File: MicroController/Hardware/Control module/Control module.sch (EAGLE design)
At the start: 101 parts, among them IC1 MCP1703CB, J1 1X2-3.5MM, J2 0446200002, J3 0446200002, J4 0446200002, Q1 BSS138, Q10 BSS138, Q11 BSS138, Q12 BSS138, Q2 BSS138, Q3 BSS138, Q4 BSS138, Q5 BSS138, Q6 BSS138, Q7 BSS138, Q8 BSS138, Q9 BSS138, U1 CD74HC4067SM96, U2 7812DT, U3 TLV1117-33CDCY, U4 CD4051BM

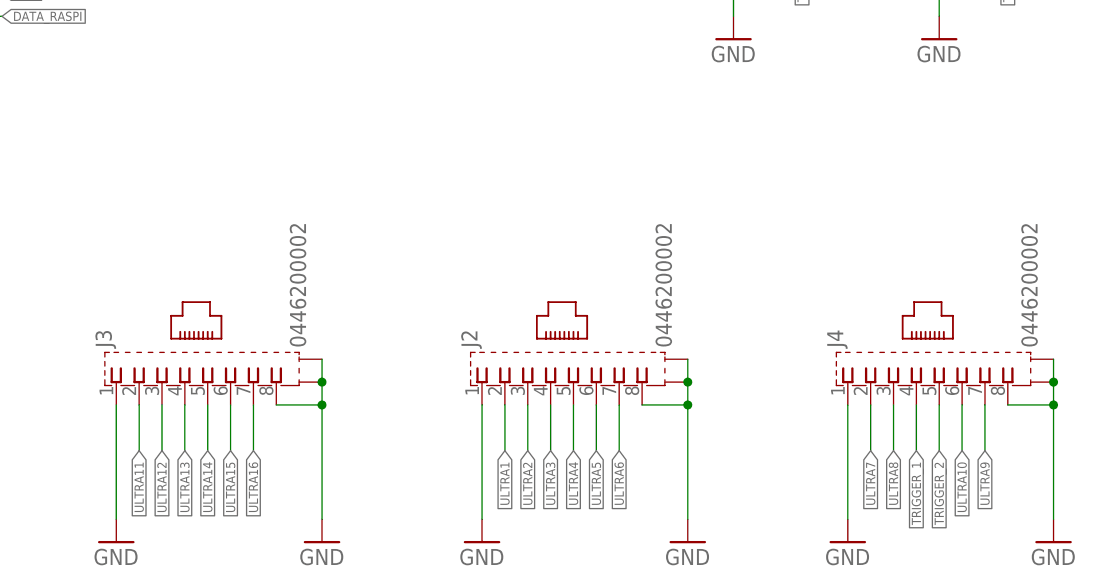
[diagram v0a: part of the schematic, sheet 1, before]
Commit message: Started a redesign of the Distance sensor PCB.
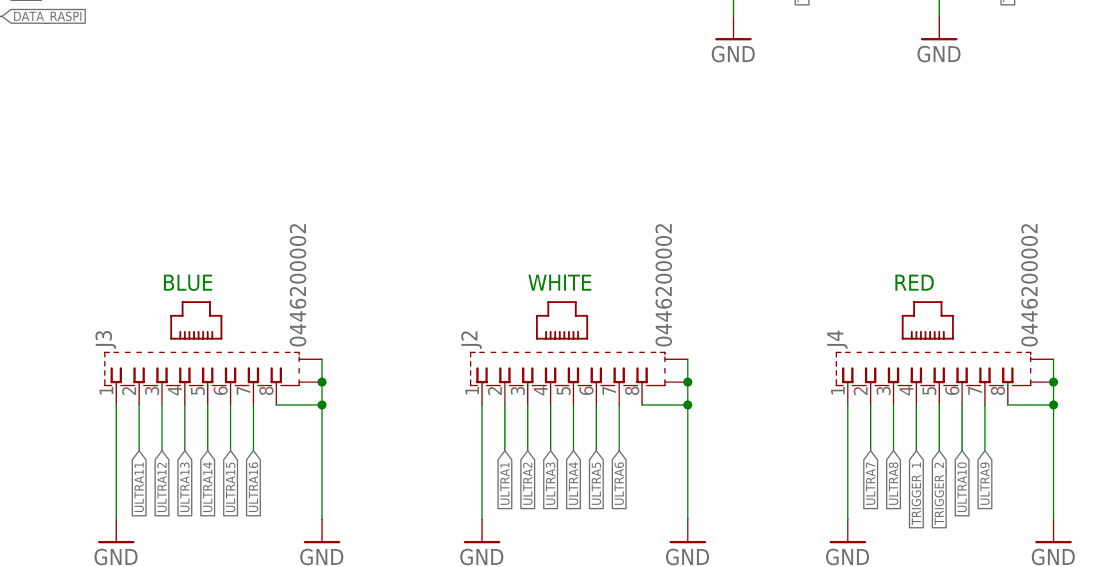
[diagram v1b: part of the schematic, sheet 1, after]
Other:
- note added: "BLUE"
- note added: "RED"
- note added: "WHITE"
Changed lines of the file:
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@@
 <text x="-2.54" y="200.66" size="1.778" layer="91">+</text>
 <text x="-2.54" y="198.12" size="1.778" layer="91">-</text>
+<text x="20.32" y="5.08" size="1.778" layer="91">BLUE</text>
+<text x="60.96" y="5.08" size="1.778" layer="91">WHITE</text>
+<text x="101.6" y="5.08" size="1.778" layer="91">RED</text>
 </plain>
 <instances>

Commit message: Started working on the next revision of the Control PCB.
Work in progress. The notes on the hardware can be found in the documentation.
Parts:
- removed C19, C20, C21, C22: 100nF, adafruit:C-USC0603
- removed FAN_1, FAN_2: JST-PH_2-PIN_HEADER, SRG:JST-PH_2-PIN_HEADER
- removed FUSE: 6V/0.5A, SparkFun-Fuses:PPTC_HALF-AMP
- removed JUMPER: (no value), jumper:JP2Q
- removed RASPBERRY: RJ11, SparkFun-Connectors:RJ11-6
- added C24: 100nF, adafruit:C-USC0805
- added FUSE1: 6V/0.5A, SparkFun-Fuses:PPTC_HALF-AMP
- added J5: 0446200002, con-molex:0446200002
- added U5: TB6621FNG, SparkFun:TB6621FNG
- added U6, U7: TXB0108PWR, Texas Instruments_By_element14_Batch_1:TXB0108PWR
- C11, C12, C13, C14, C15, C16, C17, C18: device adafruit:C-USC0603 -> adafruit:C-USC1206
- R23, R24, R25: device SparkFun:RESISTOR0603-RES -> adafruit:R-US_R0805
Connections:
- removed net DATA_RASPI: JUMPER.2, RASPBERRY.1
- removed net RES_RASPI: JUMPER.4, RASPBERRY.4
- removed net ULTRA10: J4.6, U1.CHAN4
- removed net ULTRA9: J4.7, U1.CHAN5
- new net N$10: U7.A7
- new net N$11: U7.A8
- new net N$4: U7.A1
- new net N$5: U7.A2
- new net N$6: U7.A3
- new net N$7: U7.A4
- new net N$8: U7.A5
- new net N$9: U7.A6
- new net ULTRAS1: J4.2, U6.B1
- new net ULTRAS10: U7.B2
- new net ULTRAS11: U7.B3
- new net ULTRAS12: U7.B4
- new net ULTRAS13: U7.B5
- new net ULTRAS14: U7.B6
- new net ULTRAS15: U7.B7
- new net ULTRAS16: U7.B8
- new net ULTRAS2: J4.3, U6.B2
- new net ULTRAS3: J4.4, U6.B3
- new net ULTRAS4: J4.5, U6.B4
- new net ULTRAS5: J4.6, U6.B5
- new net ULTRAS6: J4.7, U6.B6
- new net ULTRAS7: J2.2, U6.B7
- new net ULTRAS8: J2.3, U6.B8
- new net ULTRAS9: U7.B1
- net +12V: now also C24.1
- net +24V: now also FUSE1.2; no longer FUSE.2
- net A: now also U$1.PF2(OC0C/RXD0); no longer U$1.PE7(TOSC1/CKOUT/EVO/TXD1/SCK)
- net B: now also U$1.PF1(OC0B/XCK0); no longer U$1.PE6(TOSC2/RXD1/MISO)
- net C: now also U$1.PF0(OC0A); no longer U$1.PE5(OC1B/XCK1/MOSI)
- net FAN_1_CONTROL: now also U5.PWMA; no longer FAN_1.2
- net FAN_2_CONTROL: now also U5.PWMB; no longer FAN_2.2
- net GND: now also C24.2, J5.1, J5.3, J5.5, J5.7, J5.S1, J5.S2, U5.GND, U6.GND, U7.GND; no longer C19.2, C20.2, C21.2, C22.2, FAN_1.1, FAN_2.1, RASPBERRY.2
- net IR_3: now also U$1.PA2(ADC2/AC2)
- net IR_4: now also U$1.PA3(ADC3/AC3)
- net IR_5: no longer U$1.PA2(ADC2/AC2)
- net IR_6: no longer U$1.PA3(ADC3/AC3)
- net LED_1: now also U$1.PF3(OC0D/TXD0); no longer U$1.PD4(OC1A/SS)
- net LED_2: now also U$1.PF4; no longer U$1.PD5(OC1B/XCK1/MOSI)
- net MOTOR_LEVEL_3: now also U4.6; no longer U4.4
- net MOTOR_LEVEL_4: now also U4.4; no longer U4.6
- net PDI_DATA: no longer JUMPER.1
- net RESET_PDI_CLK: no longer JUMPER.3
- net RX_RASPI: now also J5.4; no longer RASPBERRY.5
- net TEMP_1: now also U$1.PD6(RXD1/MISO); no longer U$1.PF3(OC0D/TXD0)
- net TEMP_2: now also U$1.PD5(OC1B/XCK1/MOSI); no longer U$1.PF4
- net TEMP_3: now also U$1.PD4(OC1A/SS); no longer U$1.PF5
- net TRIGGER_1: no longer J4.4
- net TRIGGER_2: no longer J4.5
- net TX_RASPI: now also J5.6; no longer RASPBERRY.3
- net ULTRA1: now also U1.CHAN0, U6.A1; no longer J2.2, U1.CHAN3
- net ULTRA11: no longer U1.CHAN10
- net ULTRA2: now also U1.CHAN1, U6.A2; no longer J2.3, U1.CHAN2
- net ULTRA3: now also U1.CHAN2, U6.A3; no longer U1.CHAN1
- net ULTRA4: now also U1.CHAN3, U6.A4; no longer U1.CHAN0
- net ULTRA5: now also U1.CHAN4, U6.A5; no longer U1.CHAN8
- net ULTRA6: now also U1.CHAN5, U6.A6; no longer U1.CHAN9
- net ULTRA7: now also U6.A7; no longer J4.2, U1.CHAN7
- net ULTRA8: now also U6.A8; no longer J4.3, U1.CHAN6
- net VCC: now also J5.2, J5.8, U6.OE, U6.VCCA, U7.OE, U7.VCCA; no longer C19.1, C20.1, C21.1, C22.1, RASPBERRY.6
- net VIN: now also FUSE1.1; no longer FUSE.1
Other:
- moved on the sheet: C1, C10, C11, C12, C13, C14, C15, C16, C17, C18, C2, C23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

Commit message: Control PCB revision 2 is now complete.
A lot of changes compared to the first revision. Most noticable the layout of the connectors and the addition of the motor driver.
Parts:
- removed IC1: MCP1703CB, linear:MCP1703CB
- removed IR_1, IR_2, IR_3, IR_4, IR_5, IR_6, IR_7, IR_8: JST-PH_3-PIN_HEADER, SRG:JST-PH_3-PIN_HEADER
- removed MOTOR_1, MOTOR_2, MOTOR_3, MOTOR_4, MOTOR_5, MOTOR_6, MOTOR_7, MOTOR_8: JST-PH_2-PIN_HEADER, SRG:JST-PH_2-PIN_HEADER
- removed U$1: XMEGA-A3-AU, SparkFun-Retired:XMEGA-A3-AU
- added 12V, FAN_1, FAN_2: 1X2-3.5MM, adafruit:1X2-3.5MM
- added C19, C20, C21, C25, C26: 1.0uF, SparkFun-Capacitors:1.0UF-0805-25V-(+80/-20%)
- added C22: 1.0uF, SparkFun-Capacitors:1.0UF-0805-25V-10%
- added FUSE2: 6V/0.5A, SparkFun-Fuses:PPTC_HALF-AMP
- added LED3: (no value), adafruit:LEDCHIPLED_0805
- added MOTOR1, MOTOR2, MOTOR3, MOTOR4, MOTOR5, MOTOR6, MOTOR7, MOTOR8: 22-05-7028-02, con-molex:22-05-7028-02
- added R30: 330, adafruit:R-US_R0805
- added SENSOR1, SENSOR2, SENSOR3, SENSOR4, SENSOR5, SENSOR6, SENSOR7, SENSOR8: 22-05-7038-03, con-molex:22-05-7038-03
- added U8: LM2937IMP-5.0, NSC_By_element14_Batch_1.1:LM2937IMP-5.0
- added U9: CD74HC4067SM96, SparkFun-IC-Logic:74HC4067SM96
- C10, C6, C7, C8, C9: value 100nF -> 1.0uF; device adafruit:C-USC0805 -> SparkFun-Capacitors:1.0UF-0805-25V-(+80/-20%)
- C11, C12, C13, C14, C15, C16, C17, C18: value 100nF -> 1.0uF; device adafruit:C-USC1206 -> SparkFun-Capacitors:1.0UF-0805-25V-10%
- C2: value 220pF -> 1.0uF; device adafruit:C-USC1206 -> SparkFun-Capacitors:1.0UF-0805-25V-10%
- C24: value 100nF -> 1.0uF; device adafruit:C-USC0805 -> SparkFun-Capacitors:1.0UF-0805-25V-10%
- C3: value 100nF -> 1.0uF; device adafruit:C-USC1206 -> SparkFun-Capacitors:1.0UF-0805-25V-(+80/-20%)
- LED1, LED2: device led:LEDCHIPLED_0805 -> adafruit:LEDCHIPLED_0805
- U1: value CD74HC4067SM96 -> XMEGA-A3-AU; device SparkFun-IC-Logic:74HC4067SM96 -> SparkFun-Retired:XMEGA-A3-AU
- renumbered J1 to 24V, J5 to COMMUNICATION
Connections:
- removed net MOTOR_CONTROL: U$1.PD3(OX0D/TXD0), U4.COM_OUT/IN
- removed net N$10: U7.A7
- removed net N$11: U7.A8
- removed net N$5: U7.A2
- removed net N$6: U7.A3
- removed net N$8: U7.A5
- removed net N$9: U7.A6
- new net 12V_FANS: C22.1, C24.1, FUSE2.2, U5.VM1, U5.VM2, U5.VM3
- new net FAN_1+: FAN_1.1, U5.B01@11, U5.B01@12
- new net FAN_1-: FAN_1.2, U5.B02@7, U5.B02@8
- new net FAN_2+: FAN_2.2, U5.A01@1, U5.A01@2
- new net FAN_2-: FAN_2.1, U5.A02@5, U5.A02@6
- new net LED_3: R30.2, U1.PF5
- new net MOTOR_PWM: U1.PD1(OC0B/XCK0), U4.COM_OUT/IN
- new net ULTRA10: U7.A2, U9.CHAN9
- new net ULTRA9: U7.A1, U9.CHAN8
- net +12V: now also C19.1, C21.1, COMMUNICATION.2, U8.VIN; no longer C24.1, IC1.VI
- net +5V: now also C20.1, J2.5, J2.6, U6.VCCB, U7.VCCB, U8.VOUT; no longer IC1.VO
- net A: now also U1.PF2(OC0C/RXD0); no longer U$1.PF2(OC0C/RXD0)
- net B: now also U1.PF1(OC0B/XCK0); no longer U$1.PF1(OC0B/XCK0)
- net C: now also U1.PF0(OC0A); no longer U$1.PF0(OC0A)
- net FAN_1_CONTROL: now also U1.PC0(OC0A/OC0AL/SDA); no longer U$1.PC1(OC0B/AC0AH/XCK0/SCL)
- net FAN_2_CONTROL: now also U1.PC1(OC0B/AC0AH/XCK0/SCL); no longer U$1.PC0(OC0A/OC0AL/SDA)
- net GND: now also 12V.1, C19.2, C20.2, C21.2, C22.2, C25.2, C26.2, LED3.C, MOTOR1-1.S, MOTOR2-1.S, MOTOR3-1.S, MOTOR4-1.S, MOTOR5-1.S, MOTOR6-1.S, MOTOR7-1.S, MOTOR8-1.S, SENSOR1-2.S, SENSOR2-2.S, SENSOR3-2.S, SENSOR4-2.S, SENSOR5-2.S, SENSOR6-2.S, SENSOR7-2.S, SENSOR8-2.S, U1.AGND, U1.GND1, U1.GND2, U1.GND3, U1.GND4, U1.GND5, U5.AIN2, U5.BIN2, U5.PGND1@3, U5.PGND1@4, U5.PGND2@10, U5.PGND2@9, U8.GND, U8.GND_(TAB), U9.EN, U9.GND; no longer IC1.GND, IR_1.2, IR_2.2, IR_3.2, IR_4.2, IR_5.2, IR_6.2, IR_7.2, IR_8.2, J2.1, J2.8, MOTOR_1.1, MOTOR_2.1, MOTOR_3.1, MOTOR_4.1, MOTOR_5.1, MOTOR_6.1, MOTOR_7.1, MOTOR_8.1, U$1.AGND, U$1.GND1, U$1.GND2, U$1.GND3, U$1.GND4, U$1.GND5, U1.EN, U1.GND
- net IR_1: now also SENSOR1-1.S, U1.PA0(ADC0/AC0/AREF); no longer IR_1.1, U$1.PA0(ADC0/AC0/AREF)
- net IR_2: now also SENSOR2-1.S, U1.PA1(ADC1/AC1); no longer IR_2.1, U$1.PA1(ADC1/AC1)
- net IR_3: now also SENSOR3-1.S, U1.PB2(ADC2/AC2/DAC0); no longer IR_3.1, U$1.PA2(ADC2/AC2), U$1.PA4(ADC4/AC4)
- net IR_4: now also SENSOR4-1.S, U1.PB3(ADC3/AC3/DAC1); no longer IR_4.1, U$1.PA3(ADC3/AC3), U$1.PA5(ADC5/AC5)
- net IR_5: now also SENSOR5-1.S, U1.PB4(ADC4/AC4/TMS); no longer IR_5.1
- net IR_6: now also SENSOR6-1.S, U1.PB5(ADC5/AC5/TDI); no longer IR_6.1
- net IR_7: now also SENSOR7-1.S, U1.PB6(ADC6/AC6/TCK); no longer IR_7.1, U$1.PA6(ADC6/AC6)
- net IR_8: now also SENSOR8-1.S, U1.PB7(ADC7/AC7/AC0OUT/TDO); no longer IR_8.1, U$1.PA7(ADC7/AC7/AC0OUT)
- net LED_1: now also U1.PF3(OC0D/TXD0); no longer U$1.PF3(OC0D/TXD0)
- net LED_2: now also U1.PF4; no longer U$1.PF4
- net MOTOR_1: now also MOTOR1-2.S; no longer MOTOR_1.2
- net MOTOR_2: now also MOTOR2-2.S; no longer MOTOR_2.2
- net MOTOR_3: now also MOTOR3-2.S; no longer MOTOR_3.2
- net MOTOR_4: now also MOTOR4-2.S; no longer MOTOR_4.2
- net MOTOR_5: now also MOTOR5-2.S; no longer MOTOR_5.2
- net MOTOR_6: now also MOTOR6-2.S; no longer MOTOR_6.2
- net MOTOR_7: now also MOTOR7-2.S; no longer MOTOR_7.2
- net MOTOR_8: now also MOTOR8-2.S; no longer MOTOR_8.2
- net N$4: now also LED3.A, R30.1; no longer U7.A1
- net N$7: now also 12V.2, FUSE2.1; no longer U7.A4
- net PDI_DATA: now also U1.PDI_DATA; no longer U$1.PDI_DATA
- net RESET_PDI_CLK: now also U1./RESET_PDI_CLK; no longer U$1./RESET_PDI_CLK
- net RX_ATXMEGA: now also U1.PD2(OC0C/RXD0); no longer U$1.PC2(OC0C/OC0BL/RXD0)
- net S0: now also U1.PC7(OC0DH/CKOUT/EVO/TXD1/SCK), U9.S0; no longer U$1.PC7(OC0DH/CKOUT/EVO/TXD1/SCK), U1.S0
- net S1: now also U1.PC6(OC0DL/RXD1/MISO), U9.S1; no longer U$1.PC6(OC0DL/RXD1/MISO), U1.S1
- net S2: now also U1.PC5(OC1B/OC0CH/XCK1/MOSI), U9.S2; no longer U$1.PC5(OC1B/OC0CH/XCK1/MOSI), U1.S2
- net S3: now also U1.PC4(AC1A/OC0CL/SS), U9.S3; no longer U$1.PC4(AC1A/OC0CL/SS), U1.S3
- net TEMP_1: now also U1.PD6(RXD1/MISO); no longer U$1.PD6(RXD1/MISO)
- net TEMP_2: now also U1.PD5(OC1B/XCK1/MOSI); no longer U$1.PD5(OC1B/XCK1/MOSI)
- net TEMP_3: now also U1.PD4(OC1A/SS); no longer U$1.PD4(OC1A/SS)
- net TRIGGER_1: now also J2.3
- net TRIGGER_2: now also J2.4
- net TX_ATXMEGA: now also U1.PD3(OX0D/TXD0); no longer U$1.PC3(OC0D/OX0BH/TXD0)
- net ULTRA1: now also U9.CHAN0; no longer U1.CHAN0
- net ULTRA11: now also U7.A3, U9.CHAN10; no longer J3.2
- net ULTRA12: now also U7.A4, U9.CHAN11; no longer J3.3, U1.CHAN11
- net ULTRA13: now also U7.A5, U9.CHAN12; no longer J3.4, U1.CHAN12
- net ULTRA14: now also U7.A6, U9.CHAN13; no longer J3.5, U1.CHAN13
- net ULTRA15: now also U7.A7, U9.CHAN14; no longer J3.6, U1.CHAN14
- net ULTRA16: now also U7.A8, U9.CHAN15; no longer J3.7, U1.CHAN15
- net ULTRA2: now also U9.CHAN1; no longer U1.CHAN1
- net ULTRA3: now also U9.CHAN2; no longer J2.4, U1.CHAN2
- net ULTRA4: now also U9.CHAN3; no longer J2.5, U1.CHAN3
- net ULTRA5: now also U9.CHAN4; no longer J2.6, U1.CHAN4
- net ULTRA6: now also U9.CHAN5; no longer J2.7, U1.CHAN5
- net ULTRA7: now also U9.CHAN6
- net ULTRA8: now also U9.CHAN7
- net ULTRAS10: now also J2.8
- net ULTRAS11: now also J3.2
- net ULTRAS12: now also J3.3
- net ULTRAS13: now also J3.4
- net ULTRAS14: now also J3.5
- net ULTRAS15: now also J3.6
- net ULTRAS16: now also J3.7
- net ULTRAS7: now also J2.1; no longer J2.2
- net ULTRAS8: now also J2.2; no longer J2.3
- net ULTRAS9: now also J2.7
- net ULTRA_COM: now also U1.PD0(OC0A), U9.COM; no longer U$1.PD0(OC0A), U1.COM
- net ULTRA_TRIGGER_1: now also U1.PC3(OC0D/OX0BH/TXD0); no longer U$1.PD2(OC0C/RXD0)
- net ULTRA_TRIGGER_2: now also U1.PC2(OC0C/OC0BL/RXD0); no longer U$1.PD1(OC0B/XCK0)
- net VCC: now also C25.1, C26.1, SENSOR1-3.S, SENSOR2-3.S, SENSOR3-3.S, SENSOR4-3.S, SENSOR5-3.S, SENSOR6-3.S, SENSOR7-3.S, SENSOR8-3.S, U1.AVCC, U1.VCC1, U1.VCC2, U1.VCC3, U1.VCC4, U1.VCC5, U5.AIN1, U5.BIN1, U5.STBY, U5.VCC, U9.VCC; no longer COMMUNICATION.2, IR_1.3, IR_2.3, IR_3.3, IR_4.3, IR_5.3, IR_6.3, IR_7.3, IR_8.3, U$1.AVCC, U$1.VCC1, U$1.VCC2, U$1.VCC3, U$1.VCC4, U$1.VCC5, U1.VCC
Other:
- moved on the sheet: C10, C11, C12, C13, C14, C15, C16, C17, C18, C2, C23, C24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

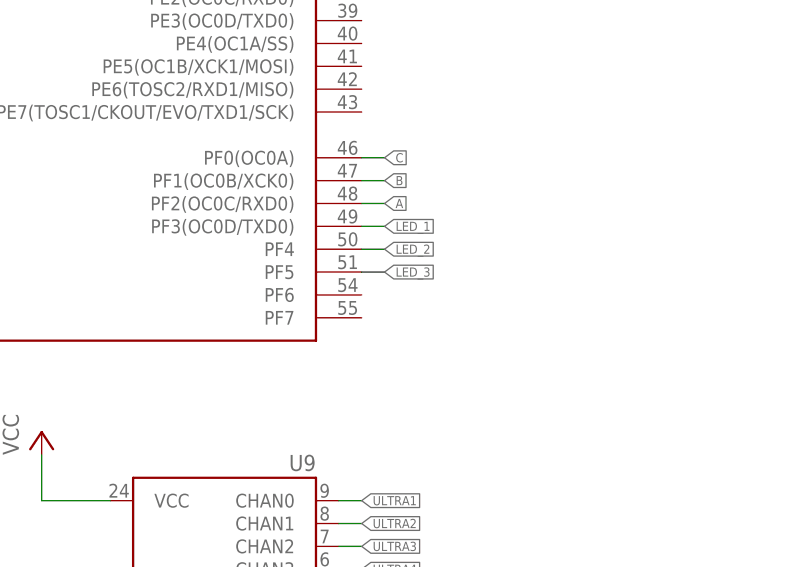
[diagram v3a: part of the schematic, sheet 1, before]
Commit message: Moved the LED connection to another pin.
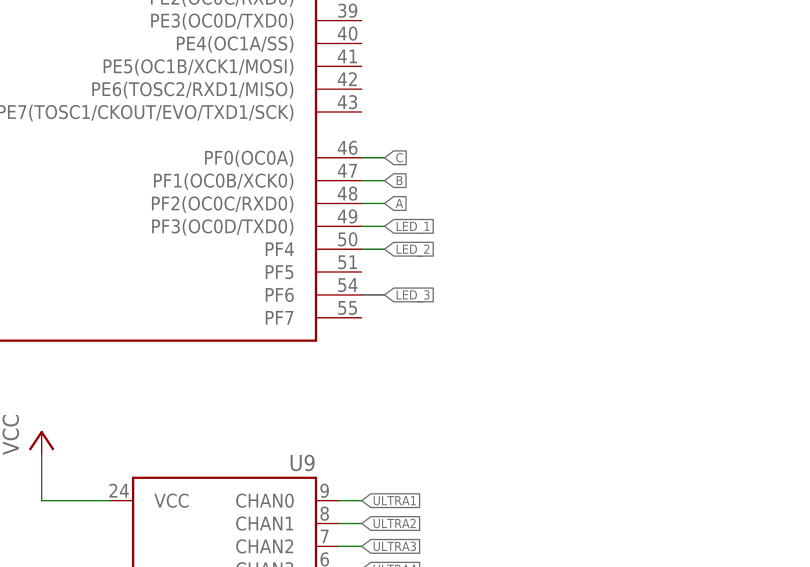
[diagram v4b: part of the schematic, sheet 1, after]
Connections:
- net LED_3: now also U1.PF6; no longer U1.PF5
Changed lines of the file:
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@@
 <net name="LED_3" class="0">
-<segment>
-<pinref part="U1" gate="G$1" pin="PF5"/>
-<wire x1="172.72" y1="116.84" x2="175.26" y2="116.84" width="0.1524" layer="91"/>
-<label x="175.26" y="116.84" size="1.016" layer="95" xref="yes"/>
-</segment>
 <segment>
 <pinref part="R30" gate="G$1" pin="2"/>
@@
 <label x="243.84" y="162.56" size="1.016" layer="95" rot="R180" xref="yes"/>
 </segment>
+<segment>
+<pinref part="U1" gate="G$1" pin="PF6"/>
+<wire x1="172.72" y1="114.3" x2="175.26" y2="114.3" width="0.1524" layer="91"/>
+<label x="175.26" y="114.3" size="1.016" layer="95" xref="yes"/>
+</segment>
 </net>

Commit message: Many changes in this new version of the Control PCB.
The motor drivers are replaced by MOSFET's.
The schematic is much better organized. 
Small additional changes.
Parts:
- removed 12V, 24V: 1X2-3.5MM, adafruit:1X2-3.5MM
- removed C10, C6: 1.0uF, SparkFun-Capacitors:1.0UF-0805-25V-(+80/-20%)
- removed C11, C12, C13, C14, C15, C16, C17, C18, C22, C24: 1.0uF, SparkFun-Capacitors:1.0UF-0805-25V-10%
- removed C23: 22uF, adafruit:CPOL-US153CLV-0505
- removed FUSE1, FUSE2: 6V/0.5A, SparkFun-Fuses:PPTC_HALF-AMP
- removed U2: 7812DT, adafruit:7812DT
- removed U5: TB6621FNG, SparkFun:TB6621FNG
- added D1, D2: BAT60J, diode:BAT60J
- added J1: (no value), SparkFun-Connectors:CONN_025MM
- added R31, R32: 1K, SparkFun:RESISTOR0603-RES
- added T1: SI4804CDY-T1-GE3, zetex:DMN3024LSD
- C1: value 220uF -> (none); device adafruit:CPOL-US175TMP-0810 -> adafruit:CPOL-US150CLZ-0810
- C2: value 1.0uF -> (none); device SparkFun-Capacitors:1.0UF-0805-25V-10% -> adafruit:CPOL-US150CLZ-0810
- C8: value 1.0uF -> 22uF; device SparkFun-Capacitors:1.0UF-0805-25V-(+80/-20%) -> adafruit:CPOL-US153CLV-0505
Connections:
- removed net +24V: C1.+, C2.1, FUSE1.2, U2.VI
- removed net 12V_FANS: C22.1, C24.1, FUSE2.2, U5.VM1, U5.VM2, U5.VM3
- removed net FAN_1+: FAN_1.1, U5.B01@11, U5.B01@12
- removed net FAN_1-: FAN_1.2, U5.B02@7, U5.B02@8
- removed net FAN_1_CONTROL: U1.PC0(OC0A/OC0AL/SDA), U5.PWMA
- removed net FAN_2+: FAN_2.2, U5.A01@1, U5.A01@2
- removed net FAN_2-: FAN_2.1, U5.A02@5, U5.A02@6
- removed net FAN_2_CONTROL: U1.PC1(OC0B/AC0AH/XCK0/SCL), U5.PWMB
- removed net RX_RASPI: COMMUNICATION.4, Q12.D, R29.2
- removed net TX_RASPI: COMMUNICATION.6, Q11.S, R26.2
- removed net VIN: 24V.2, FUSE1.1
- new net FAN_ROW_1_PWM: R31.1, U1.PC1(OC0B/AC0AH/XCK0/SCL)
- new net FAN_ROW_2_PWM: R32.1, U1.PC0(OC0A/OC0AL/SDA)
- new net N$2: R31.2, T1A.G
- new net N$5: D2.A, FAN_2.1, T1B.D
- new net N$6: R32.2, T1B.G
- new net RX: Q11.D, R27.2, U1.PD2(OC0C/RXD0)
- new net TX: Q12.S, R28.2, U1.PD3(OX0D/TXD0)
- net +12V: now also C1.+, C2.+, D1.C, D2.C, FAN_1.2, FAN_2.2, J1.2; no longer C23.+, C6.1, U2.VO
- net GND: now also C2.-, C8.-, J1.1, T1A.S, T1B.S; no longer 12V.1, 24V.1, C10.2, C11.2, C12.2, C13.2, C14.2, C15.2, C16.2, C17.2, C18.2, C2.2, C22.2, C23.-, C24.2, C6.2, C8.2, U2.GND, U5.AIN2, U5.BIN2, U5.GND, U5.PGND1@3, U5.PGND1@4, U5.PGND2@10, U5.PGND2@9
- net IR_1: no longer C11.1
- net IR_2: no longer C12.1
- net IR_3: now also U1.PA2(ADC2/AC2); no longer C14.1, U1.PB2(ADC2/AC2/DAC0)
- net IR_4: now also U1.PA3(ADC3/AC3); no longer C15.1, U1.PB3(ADC3/AC3/DAC1)
- net IR_5: now also U1.PA4(ADC4/AC4); no longer C13.1, U1.PB4(ADC4/AC4/TMS)
- net IR_6: now also U1.PA5(ADC5/AC5); no longer C16.1, U1.PB5(ADC5/AC5/TDI)
- net IR_7: now also U1.PA6(ADC6/AC6); no longer C17.1, U1.PB6(ADC6/AC6/TCK)
- net IR_8: now also U1.PA7(ADC7/AC7/AC0OUT); no longer C18.1, U1.PB7(ADC7/AC7/AC0OUT/TDO)
- net N$7: now also D1.A, FAN_1.1, T1A.D; no longer 12V.2, FUSE2.1
- net RX_ATXMEGA: now also COMMUNICATION.4, Q11.S, R26.2; no longer Q11.D, R27.2, U1.PD2(OC0C/RXD0)
- net TX_ATXMEGA: now also COMMUNICATION.6, Q12.D, R29.2; no longer Q12.S, R28.2, U1.PD3(OX0D/TXD0)
- net VCC: now also C8.+; no longer C10.1, C8.1, U5.AIN1, U5.BIN1, U5.STBY, U5.VCC
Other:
- note added: "Fan_Row_1"
- note added: "Fan_Row_2"
- note removed: "+"
- note removed: "-"
- note removed: "Input power screw terminal"
